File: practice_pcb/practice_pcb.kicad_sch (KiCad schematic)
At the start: 22 parts, among them J1 VEE connector, J2 From_MCU, J3 MOSFET_out, J4 Conn_01x03, J5 Conn_01x01_Socket, J6 Conn_01x01_Socket, Q4 IRF3710, U1 LDO-3.3, U5 NSi6651A

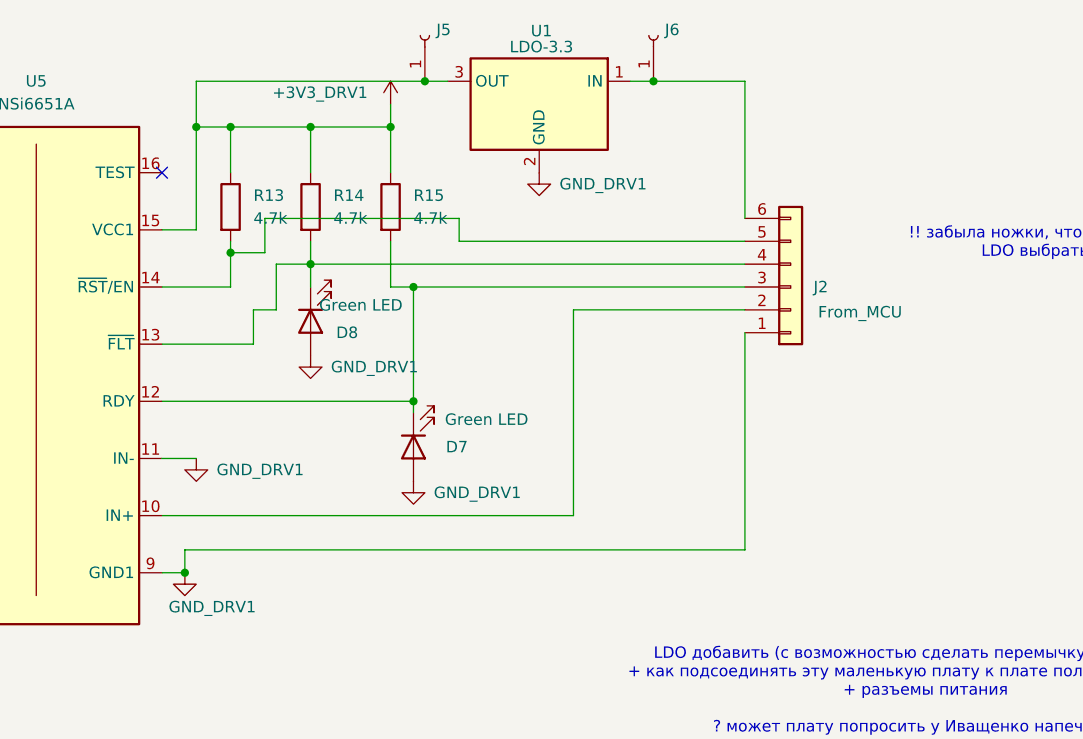
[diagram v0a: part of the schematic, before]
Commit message: practice_pcb driver schematics changed (leds).
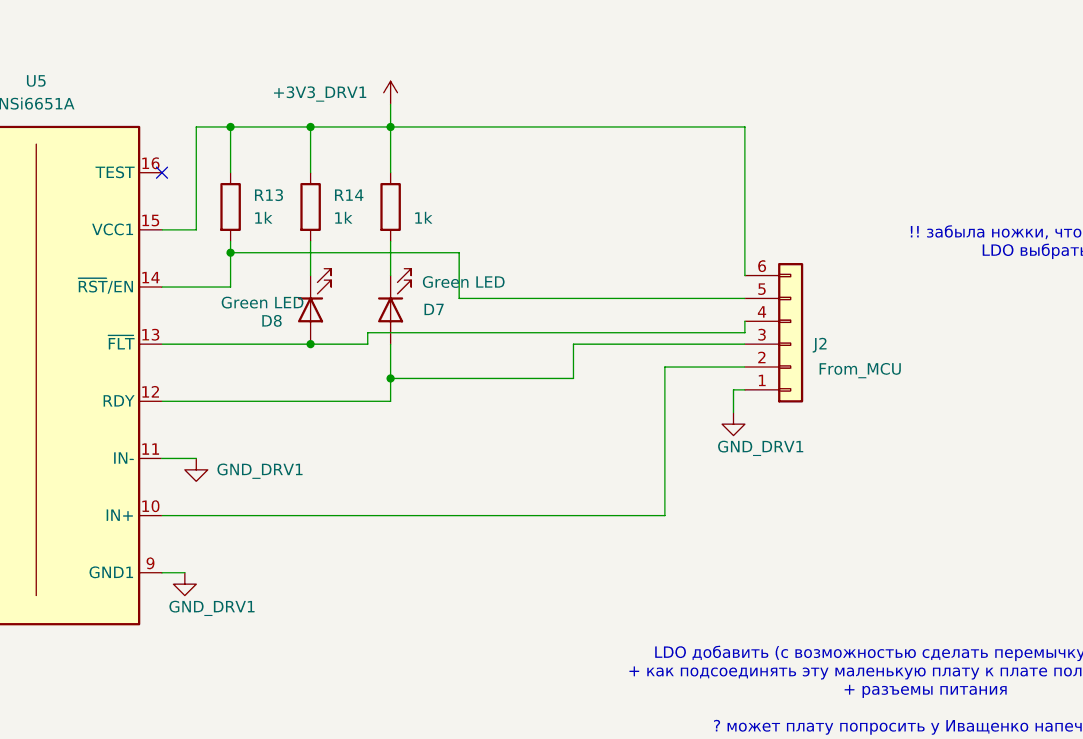
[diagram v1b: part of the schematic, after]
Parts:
- removed J5, J6: Conn_01x01_Socket, Connector_PinHeader_2.54mm:PinHeader_1x01_P2.54mm_Vertical, symbol Connector:Conn_01x01_Socket
- removed U1: LDO-3.3, Package_TO_SOT_SMD:SOT-223-3_TabPin2, symbol Regulator_Linear:LT1963AxST-3.3
- R13, R14, R15: value 4.7k -> 1k
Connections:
- net +3V3_DRV1: now also J2.6 (Pin_6)
- net GND_DRV1: no longer D7.2 (A), D8.2 (A)
- net at D8.1 (K), R14.2: no longer J2.4 (Pin_4), U5.13 (~{FLT})
- net at J2.3 (Pin_3), U5.12 (RDY): now also D7.2 (A); no longer D7.1 (K), R15.2
- new net: D8.2 (A), J2.4 (Pin_4), U5.13 (~{FLT})
- new net: D7.1 (K), R15.2
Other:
- moved on the sheet: D7, D8, J2

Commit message: Driver board: castellated holes. SMD diode.
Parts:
- removed J1: VEE connector, Connector_PinHeader_2.54mm:PinHeader_1x03_P2.54mm_Vertical, symbol Connector:Conn_01x03_Socket
- added R1, R2: 0, Resistor_SMD:R_0805_2012Metric_Pad1.20x1.40mm_HandSolder, symbol Device:R
- D10: value 1N4006 -> S1K-13-F; footprint Diode_THT:D_DO-41_SOD81_P10.16mm_Horizontal -> Diode_SMD:D_SMA
- J2: footprint TerminalBlock:TerminalBlock_Xinya_XY308-2.54-6P_1x06_P2.54mm_Horizontal -> Connector_PinHeader_2.54mm:PinHeader_1x06_P2.54mm_Vertical
- J3, J4: footprint TerminalBlock:TerminalBlock_Xinya_XY308-2.54-3P_1x03_P2.54mm_Horizontal -> Connector_PinHeader_2.54mm:PinHeader_1x03_P2.54mm_Vertical
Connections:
- net -15_DRV2: now also R1.1
- net GND_DRV2: now also R2.2
- net at U5.8 (VEE2): now also R1.2, R2.1

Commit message: Driver PCB leds error fixed.
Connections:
- net GND_DRV1: now also D7.2 (A), D8.2 (A)
- net at D8.1 (K), R14.2: now also J2.4 (Pin_4), U5.13 (~{FLT})
- net at J2.3 (Pin_3), U5.12 (RDY): now also D7.1 (K), R15.2; no longer D7.2 (A)
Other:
- moved on the sheet: D7, D8

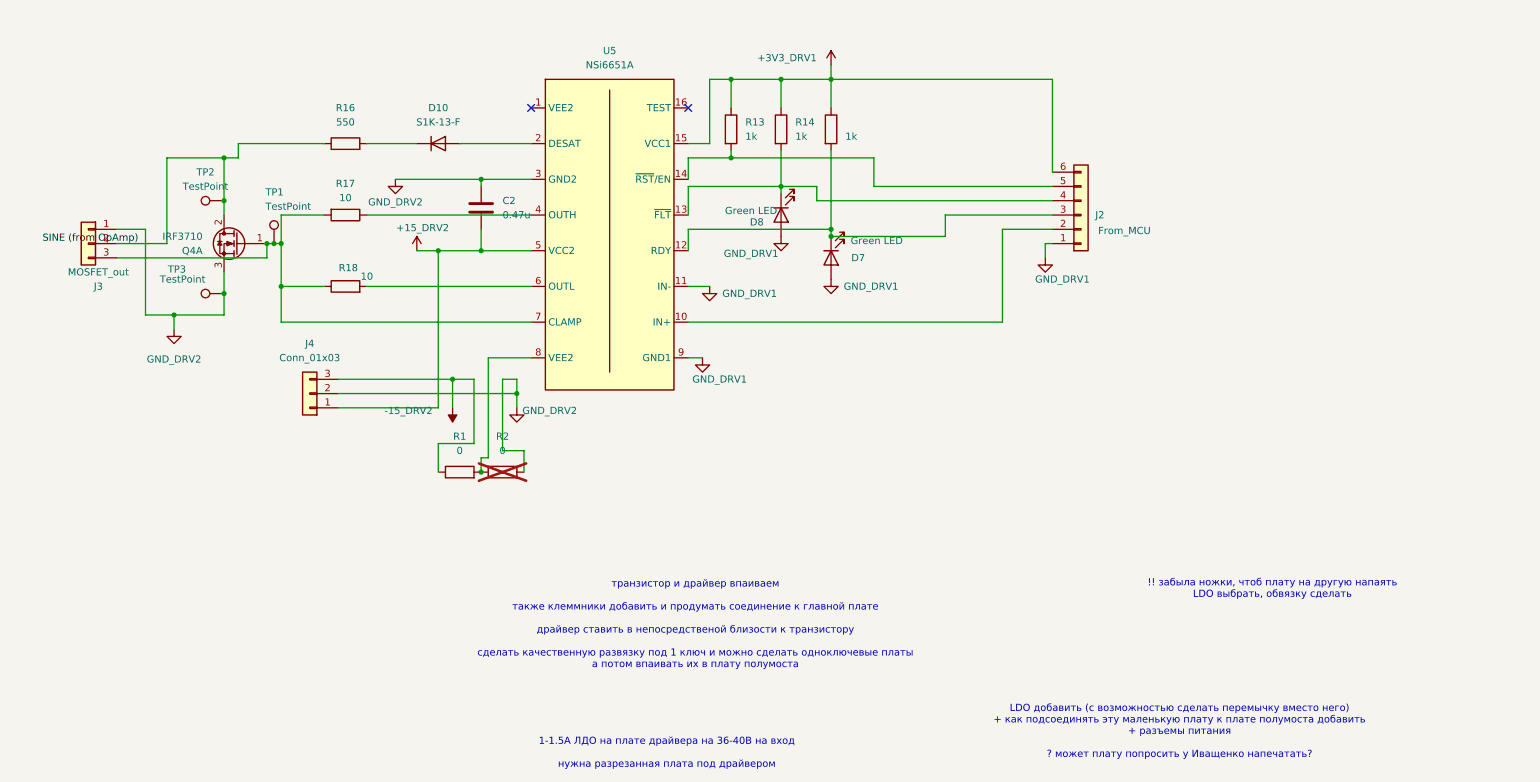
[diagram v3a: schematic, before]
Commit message: Drivers: LEDs deleted + polygon 3.3V added.
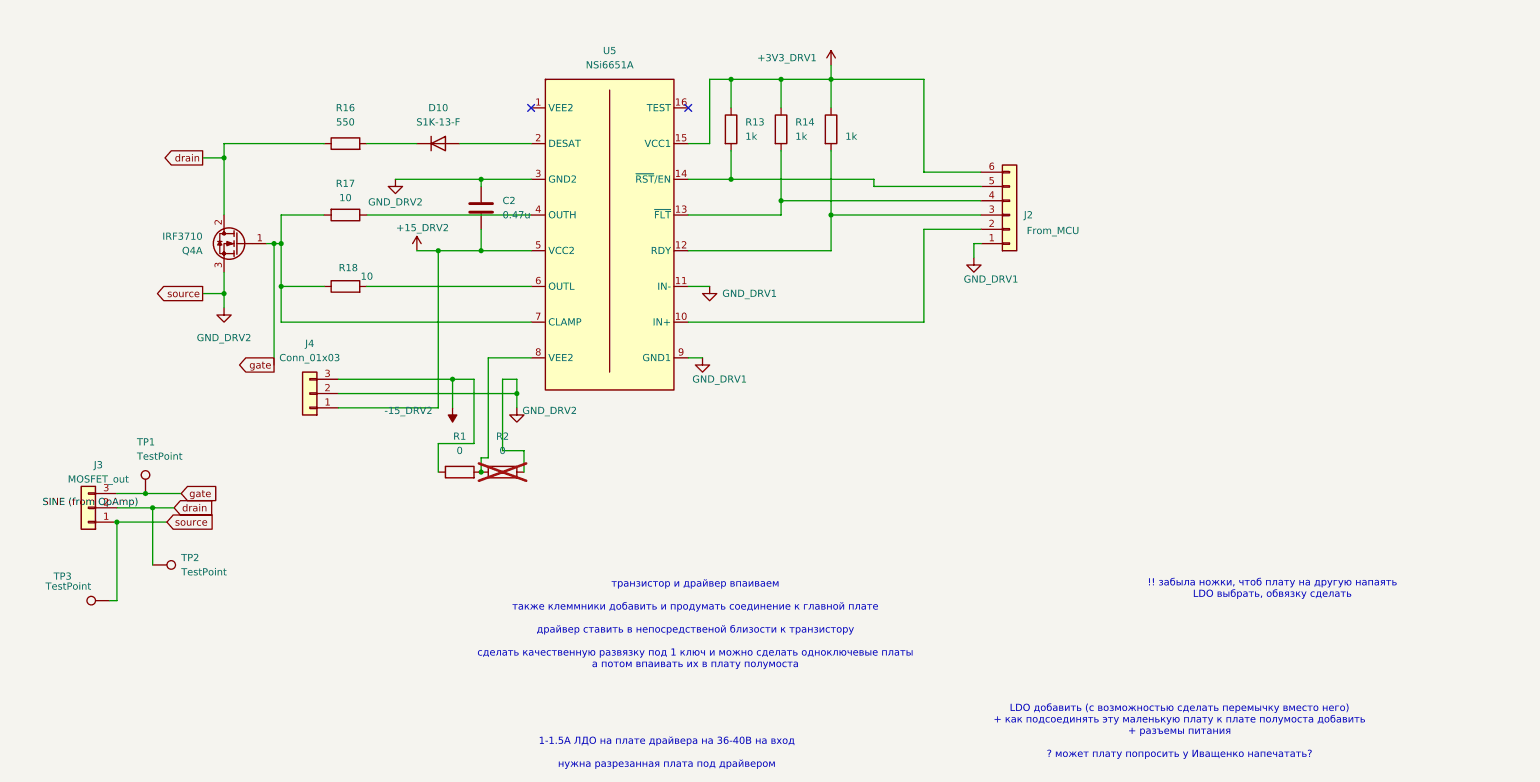
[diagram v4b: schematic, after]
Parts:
- removed D7, D8: Green LED, LED_SMD:LED_1206_3216Metric_Pad1.42x1.75mm_HandSolder, symbol Device:LED
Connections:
- net gate: now reaches J3.3 (Pin_3), Q4.1 (G), R17.2, R18.1, TP1.1, U5.7 (CLAMP)
- net SINE (from OpAmp) renamed drain
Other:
- moved on the sheet: J2
